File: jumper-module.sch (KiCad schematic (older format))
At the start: 12 parts

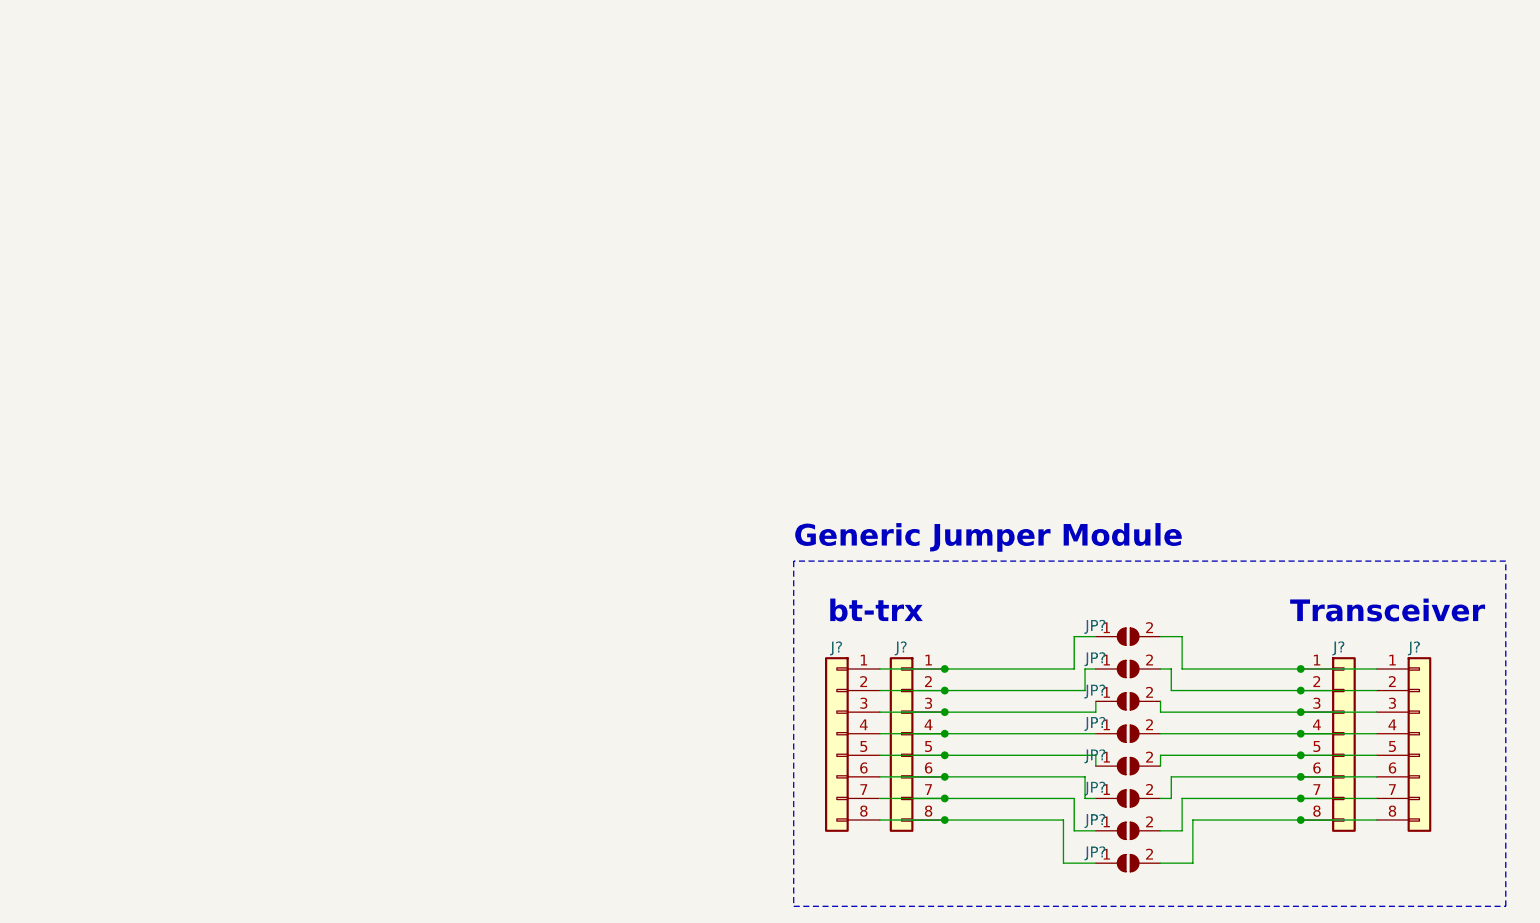
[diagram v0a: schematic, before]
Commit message: Created Generic Daughterboard
* connected 1-6 via solder jumper
* created 2x2 field for bridging GND
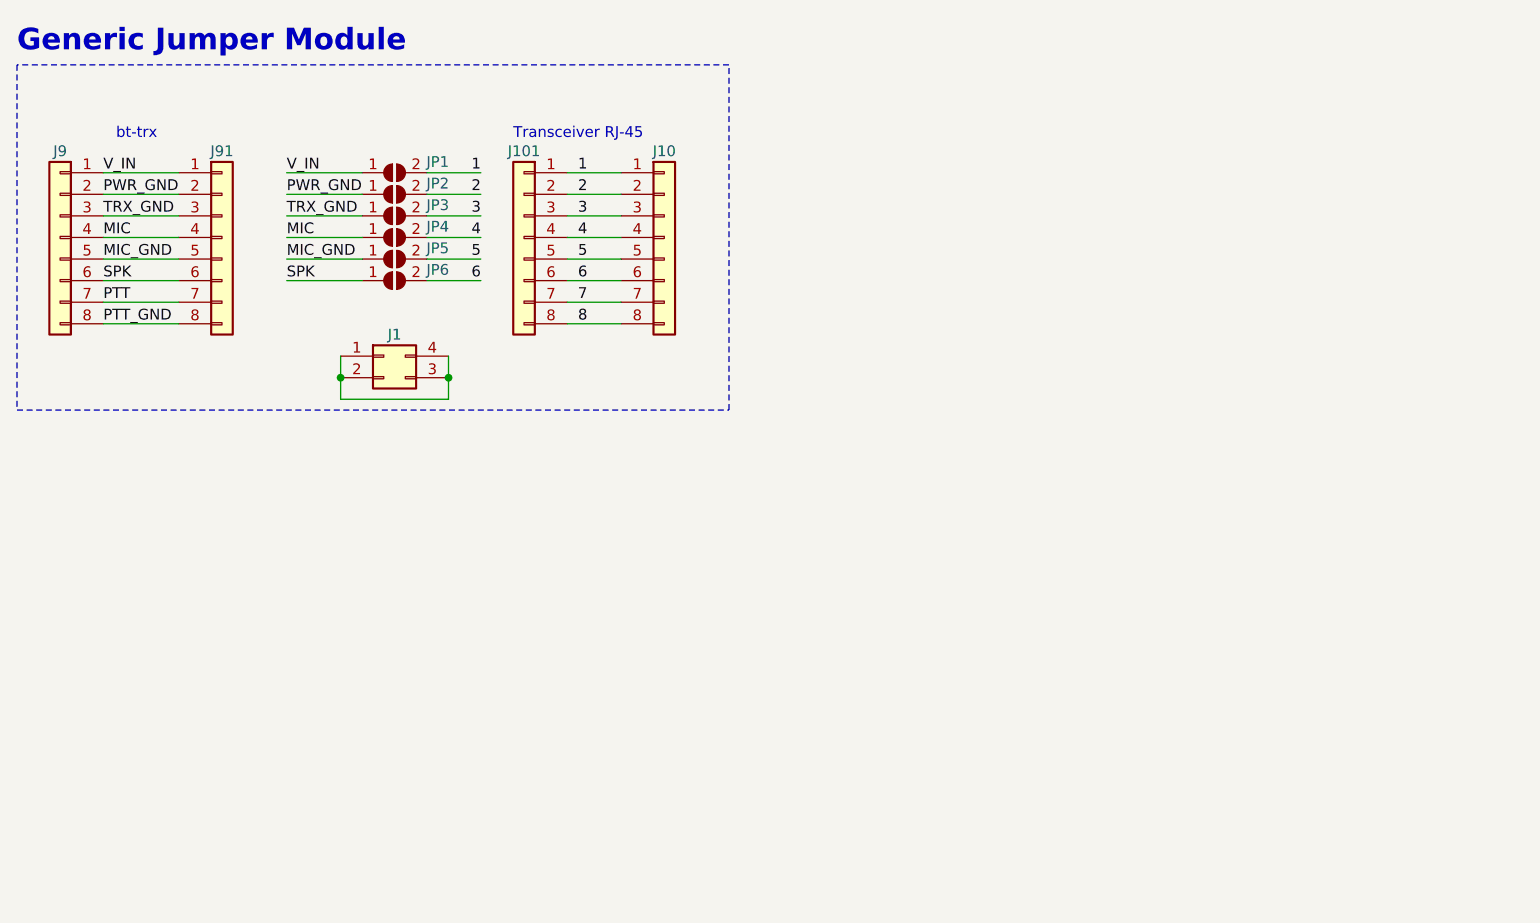
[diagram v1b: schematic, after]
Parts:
- removed J? (x2): Conn_01x08, symbol Connector_Generic:Conn_01x08
- removed JP? (x7): SolderJumper_2_Open, symbol Jumper:SolderJumper_2_Open
- added J1: (no value), Connector_PinHeader_2.54mm:PinHeader_2x02_P2.54mm_Vertical, symbol Connector_Generic:Conn_02x02_Counter_Clockwise
- added J10, J101: Conn_01x08, Connector_PinHeader_2.54mm:PinHeader_1x08_P2.54mm_Vertical, symbol Connector_Generic:Conn_01x08
- added JP2, JP3, JP4, JP5, JP6: SolderJumper_2_Open, Jumper:SolderJumper-2_P1.3mm_Open_TrianglePad1.0x1.5mm, symbol Jumper:SolderJumper_2_Open
- J9, J91: renamed from J?; footprint (none) -> Connector_PinHeader_2.54mm:PinHeader_1x08_P2.54mm_Vertical
- JP1: renamed from JP?; footprint (none) -> Jumper:SolderJumper-2_P1.3mm_Open_TrianglePad1.0x1.5mm
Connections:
- net 1: now reaches JP1.2 (B)
- net 1: now also J10.1 (Pin_1), J101.1 (Pin_1)
- net V_IN: now reaches J9.1 (Pin_1), J91.1 (Pin_1)
- net V_IN: now also JP1.1 (A)
- net PWR_GND: now reaches J9.2 (Pin_2), J91.2 (Pin_2)
- net PWR_GND: now also JP2.1 (A)
- net TRX_GND: now reaches J9.3 (Pin_3), J91.3 (Pin_3)
- net TRX_GND: now also JP3.1 (A); no longer JP1.1 (A)
- net MIC: now reaches J9.4 (Pin_4), J91.4 (Pin_4)
- net MIC: now also JP4.1 (A)
- net MIC_GND: now reaches J9.5 (Pin_5), J91.5 (Pin_5)
- net MIC_GND: now also JP5.1 (A)
- net SPK: now reaches J9.6 (Pin_6), J91.6 (Pin_6)
- net SPK: now also JP6.1 (A)
- net PTT: now reaches J9.7 (Pin_7), J91.7 (Pin_7)
- net PTT_GND: now reaches J9.8 (Pin_8), J91.8 (Pin_8)
- new net: J1.1 (Pin_1), J1.2 (Pin_2), J1.3 (Pin_3), J1.4 (Pin_4)
- new net 2: J10.2 (Pin_2), J101.2 (Pin_2), JP2.2 (B)
- new net 3: J10.3 (Pin_3), J101.3 (Pin_3), JP3.2 (B)
- new net 4: J10.4 (Pin_4), J101.4 (Pin_4), JP4.2 (B)
- new net 5: J10.5 (Pin_5), J101.5 (Pin_5), JP5.2 (B)
- new net 6: J10.6 (Pin_6), J101.6 (Pin_6), JP6.2 (B)
- new net 7: J10.7 (Pin_7), J101.7 (Pin_7)
- new net 8: J10.8 (Pin_8), J101.8 (Pin_8)
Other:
- note added: "Transceiver RJ-45"
- note removed: "Transceiver"
- moved on the sheet: J9, J91, JP1

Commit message: Added BOM
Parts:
- J1, J101, J91, JP1, JP2, JP3, JP4, JP5, JP6: Mouser-Best. Nr (none) -> -
- J10, J9: Mouser-Best. Nr (none) -> 649-68000-408HLF
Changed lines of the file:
@@
 F 2 "Connector_PinHeader_2.54mm:PinHeader_1x08_P2.54mm_Vertical" H 1700 1700 50  0001 C CNN
 F 3 "~" H 1700 1700 50  0001 C CNN
+F 4 "-" H 1700 1700 50  0001 C CNN "Mouser-Best. Nr"
 	1    1700 1700
 	1    0    0    -1
@@
 F 2 "Connector_PinHeader_2.54mm:PinHeader_1x08_P2.54mm_Vertical" H 950 1700 50  0001 C CNN
 F 3 "~" H 950 1700 50  0001 C CNN
+F 4 "649-68000-408HLF" H 950 1700 50  0001 C CNN "Mouser-Best. Nr"
 	1    950  1700
 	-1   0    0    -1
@@
 F 2 "Connector_PinHeader_2.54mm:PinHeader_1x08_P2.54mm_Vertical" H 3750 1700 50  0001 C CNN
 F 3 "~" H 3750 1700 50  0001 C CNN
+F 4 "649-68000-408HLF" H 3750 1700 50  0001 C CNN "Mouser-Best. Nr"
 	1    3750 1700
 	1    0    0    -1
@@
 F 2 "Connector_PinHeader_2.54mm:PinHeader_1x08_P2.54mm_Vertical" H 3100 1700 50  0001 C CNN
 F 3 "~" H 3100 1700 50  0001 C CNN
+F 4 "-" H 3100 1700 50  0001 C CNN "Mouser-Best. Nr"
 	1    3100 1700
 	-1   0    0    -1
@@
 F 2 "Jumper:SolderJumper-2_P1.3mm_Open_TrianglePad1.0x1.5mm" H 2500 1400 50  0001 C CNN
 F 3 "~" H 2500 1400 50  0001 C CNN
+F 4 "-" H 2500 1400 50  0001 C CNN "Mouser-Best. Nr"
 	1    2500 1400
 	1    0    0    -1
@@
 F 2 "Jumper:SolderJumper-2_P1.3mm_Open_TrianglePad1.0x1.5mm" H 2500 1500 50  0001 C CNN
 F 3 "~" H 2500 1500 50  0001 C CNN
+F 4 "-" H 2500 1500 50  0001 C CNN "Mouser-Best. Nr"
 	1    2500 1500
 	1    0    0    -1
@@
 F 2 "Jumper:SolderJumper-2_P1.3mm_Open_TrianglePad1.0x1.5mm" H 2500 1600 50  0001 C CNN
 F 3 "~" H 2500 1600 50  0001 C CNN
+F 4 "-" H 2500 1600 50  0001 C CNN "Mouser-Best. Nr"
 	1    2500 1600
 	1    0    0    -1
@@
 F 2 "Jumper:SolderJumper-2_P1.3mm_Open_TrianglePad1.0x1.5mm" H 2500 1700 50  0001 C CNN
 F 3 "~" H 2500 1700 50  0001 C CNN
+F 4 "-" H 2500 1700 50  0001 C CNN "Mouser-Best. Nr"
 	1    2500 1700
 	1    0    0    -1
@@
 F 2 "Jumper:SolderJumper-2_P1.3mm_Open_TrianglePad1.0x1.5mm" H 2500 1800 50  0001 C CNN
 F 3 "~" H 2500 1800 50  0001 C CNN
+F 4 "-" H 2500 1800 50  0001 C CNN "Mouser-Best. Nr"
 	1    2500 1800
 	1    0    0    -1
@@
 F 2 "Jumper:SolderJumper-2_P1.3mm_Open_TrianglePad1.0x1.5mm" H 2500 1900 50  0001 C CNN
 F 3 "~" H 2500 1900 50  0001 C CNN
+F 4 "-" H 2500 1900 50  0001 C CNN "Mouser-Best. Nr"
 	1    2500 1900
 	1    0    0    -1
@@
 F 2 "Connector_PinHeader_2.54mm:PinHeader_2x02_P2.54mm_Vertical" H 2450 2250 50  0001 C CNN
 F 3 "~" H 2450 2250 50  0001 C CNN
+F 4 "-" H 2450 2250 50  0001 C CNN "Mouser-Best. Nr"
 	1    2450 2250
 	1    0    0    -1

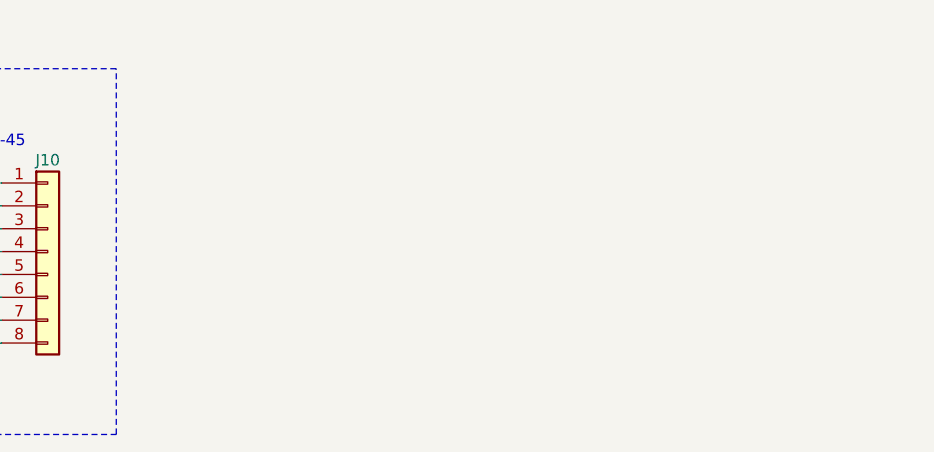
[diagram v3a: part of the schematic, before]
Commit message: Non generic Handheld JM
Created first verion of non generic handheld jumper module
for kenwood handhelds
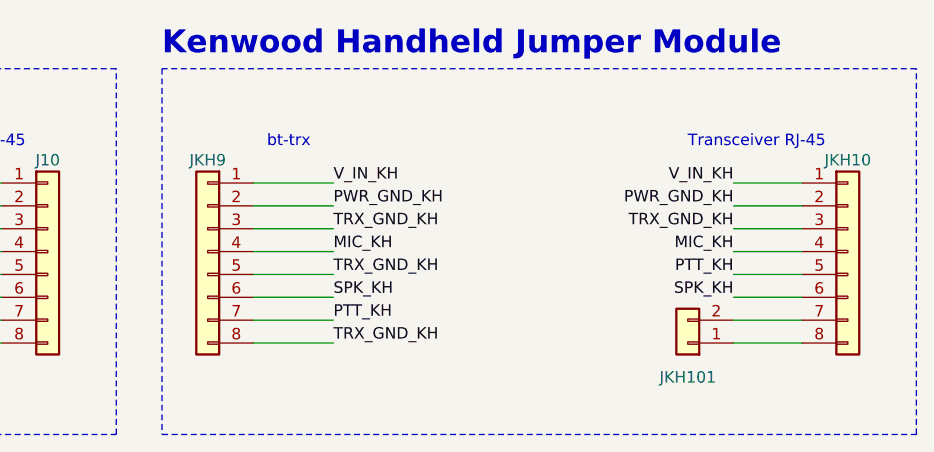
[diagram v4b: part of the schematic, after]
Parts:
- added JKH10, JKH9: Conn_01x08, Connector_PinHeader_2.54mm:PinHeader_1x08_P2.54mm_Vertical, symbol Connector_Generic:Conn_01x08
- added JKH101: Conn_01x02, Connector_PinHeader_2.54mm:PinHeader_1x02_P2.54mm_Vertical, symbol Connector_Generic:Conn_01x02
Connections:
- new net: JKH10.7 (Pin_7), JKH101.2 (Pin_2)
- new net: JKH10.8 (Pin_8), JKH101.1 (Pin_1)
- new net MIC_KH: JKH10.4 (Pin_4), JKH9.4 (Pin_4)
- new net PTT_KH: JKH10.5 (Pin_5), JKH9.7 (Pin_7)
- new net PWR_GND_KH: JKH10.2 (Pin_2), JKH9.2 (Pin_2)
- new net SPK_KH: JKH10.6 (Pin_6), JKH9.6 (Pin_6)
- new net TRX_GND_KH: JKH10.3 (Pin_3), JKH9.3 (Pin_3), JKH9.5 (Pin_5), JKH9.8 (Pin_8)
- new net V_IN_KH: JKH10.1 (Pin_1), JKH9.1 (Pin_1)
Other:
- note added: "Kenwood Handheld Jumper Module"
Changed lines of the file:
@@
 	2750 2450 2750 2350
 Connection ~ 2750 2350
+Text Notes 6550 1250 0    50   ~ 0
+Transceiver RJ-45
+Text Notes 4900 1250 2    50   ~ 0
+bt-trx
+$Comp
+L Connector_Generic:Conn_01x08 JKH9
+U 1 1 5E2D8D3B
+P 4450 1700
+F 0 "JKH9" H 4450 2100 50  0000 C CNN
+F 1 "Conn_01x08" H 4368 2126 50  0001 C CNN
+F 2 "Connector_PinHeader_2.54mm:PinHeader_1x08_P2.54mm_Vertical" H 4450 1700 50  0001 C CNN
+F 3 "~" H 4450 1700 50  0001 C CNN
+F 4 "649-68000-408HLF" H 4450 1700 50  0001 C CNN "Mouser-Best. Nr"
+	1    4450 1700
+	-1   0    0    -1
+$EndComp
+Wire Notes Line
+	4250 900  4250 2500
+Wire Notes Line
+	4250 2500 7550 2500
+Wire Notes Line
+	7550 2500 7550 900
+Wire Notes Line
+	7550 900  4250 900
+Text Notes 4250 850  0    100  ~ 20
+Kenwood Handheld Jumper Module
+$Comp
+L Connector_Generic:Conn_01x08 JKH10
+U 1 1 5E2D8D47
+P 7250 1700
+F 0 "JKH10" H 7250 2100 50  0000 C CNN
+F 1 "Conn_01x08" H 7168 2126 50  0001 C CNN
+F 2 "Connector_PinHeader_2.54mm:PinHeader_1x08_P2.54mm_Vertical" H 7250 1700 50  0001 C CNN
+F 3 "~" H 7250 1700 50  0001 C CNN
+F 4 "649-68000-408HLF" H 7250 1700 50  0001 C CNN "Mouser-Best. Nr"
+	1    7250 1700
+	1    0    0    -1
+$EndComp
+Text Label 5000 1400 0    50   ~ 0
+V_IN_KH
+Text Label 5000 1500 0    50   ~ 0
+PWR_GND_KH
+Text Label 5000 1700 0    50   ~ 0
+MIC_KH
+Text Label 5000 1800 0    50   ~ 0
+TRX_GND_KH
+Text Label 5000 1900 0    50   ~ 0
+SPK_KH
+Text Label 5000 2000 0    50   ~ 0
+PTT_KH
+Text Label 5000 1600 0    50   ~ 0
+TRX_GND_KH
+Wire Wire Line
+	4650 1400 5000 1400
+Wire Wire Line
+	4650 1500 5000 1500
+Wire Wire Line
+	4650 1600 5000 1600
+Wire Wire Line
+	4650 1700 5000 1700
+Wire Wire Line
+	4650 1800 5000 1800
+Wire Wire Line
+	4650 1900 5000 1900
+Wire Wire Line
+	4650 2000 5000 2000
+Wire Wire Line
+	4650 2100 5000 2100
+Wire Wire Line
+	7050 1400 6750 1400
+Wire Wire Line
+	7050 1500 6750 1500
+Wire Wire Line
+	7050 1600 6750 1600
+Wire Wire Line
+	7050 1700 6750 1700
+Wire Wire Line
+	7050 1800 6750 1800
+Wire Wire Line
+	7050 1900 6750 1900
+Wire Wire Line
+	7050 2000 6750 2000
+Wire Wire Line
+	7050 2100 6750 2100
+Text Label 6750 1400 2    50   ~ 0
+V_IN_KH
+Text Label 6750 1500 2    50   ~ 0
+PWR_GND_KH
+Text Label 6750 1700 2    50   ~ 0
+MIC_KH
+Text Label 6750 1900 2    50   ~ 0
+SPK_KH
+Text Label 6750 1600 2    50   ~ 0
+TRX_GND_KH
+Text Label 5000 2100 0    50   ~ 0
+TRX_GND_KH
+Text Label 6750 1800 2    50   ~ 0
+PTT_KH
+$Comp
+L Connector_Generic:Conn_01x02 JKH101
+U 1 1 5E334DDE
+P 6550 2100
+F 0 "JKH101" H 6550 2250 50  0000 C CNN
+F 1 "Conn_01x02" H 6550 2250 50  0001 C CNN
+F 2 "Connector_PinHeader_2.54mm:PinHeader_1x02_P2.54mm_Vertical" H 6550 2100 50  0001 C CNN
+F 3 "~" H 6550 2100 50  0001 C CNN
+	1    6550 2100
+	-1   0    0    1
+$EndComp
 $EndSCHEMATC
